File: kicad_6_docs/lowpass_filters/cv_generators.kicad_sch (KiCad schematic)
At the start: 28 parts, among them U6 TL072, U7 TL072

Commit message: Initial filter board layout
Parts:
- R1, R10: value 100k -> 330k
- R11, R2: value 330k -> 680k
- RV1, RV3, RV4: value 10k -> 100k
- RV2: value 10k_C.D. -> 100k_C.D.
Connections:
- net +5VA renamed +15V
- net -5VA renamed -15V
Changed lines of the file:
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@@
       (effects (font (size 1.27 1.27)) (justify right))
     )
-    (property "Value" "10k" (id 1) (at 43.18 123.1899 0)
+    (property "Value" "100k" (id 1) (at 43.18 123.1899 0)
       (effects (font (size 1.27 1.27)) (justify right))
     )
@@
       (effects (font (size 1.27 1.27)) (justify right))
     )
-    (property "Value" "10k" (id 1) (at 43.18 162.5599 0)
+    (property "Value" "100k" (id 1) (at 43.18 162.5599 0)
       (effects (font (size 1.27 1.27)) (justify right))
     )
@@
     (pin "3")
   )
+  (symbol (lib_id "power:-15V") (at 45.72 87.63 180) (unit 1)
+    (in_bom yes) (on_board yes) (fields_autoplaced)
+    (property "Reference" "#PWR?" (id 0) (at 45.72 90.17 0)
+      (effects (font (size 1.27 1.27)) hide)
+    )
+    (property "Value" "-15V" (id 1) (at 45.72 92.71 0))
+    (property "Footprint" "" (id 2) (at 45.72 87.63 0)
+      (effects (font (size 1.27 1.27)) hide)
+    )
+    (property "Datasheet" "" (id 3) (at 45.72 87.63 0)
+      (effects (font (size 1.27 1.27)) hide)
+    )
+    (pin "1")
+  )
   (symbol (lib_id "Device:R_Potentiometer") (at 45.72 81.28 0) (mirror x) (unit 1)
     (in_bom yes) (on_board yes) (fields_autoplaced)
@@
       (effects (font (size 1.27 1.27)) (justify right))
     )
-    (property "Value" "10k_C.D." (id 1) (at 43.18 82.5499 0)
+    (property "Value" "100k_C.D." (id 1) (at 43.18 82.5499 0)
       (effects (font (size 1.27 1.27)) (justify right))
     )
@@
     (pin "2")
   )
+  (symbol (lib_id "power:+15V") (at 45.72 106.68 0) (unit 1)
+    (in_bom yes) (on_board yes) (fields_autoplaced)
+    (property "Reference" "#PWR?" (id 0) (at 45.72 110.49 0)
+      (effects (font (size 1.27 1.27)) hide)
+    )
+    (property "Value" "+15V" (id 1) (at 45.72 101.6 0))
+    (property "Footprint" "" (id 2) (at 45.72 106.68 0)
+      (effects (font (size 1.27 1.27)) hide)
+    )
+    (property "Datasheet" "" (id 3) (at 45.72 106.68 0)
+      (effects (font (size 1.27 1.27)) hide)
+    )
+    (pin "1")
+  )
   (symbol (lib_id "Device:R") (at 142.24 63.5 90) (unit 1)
     (in_bom yes) (on_board yes) (fields_autoplaced)
@@
     (pin "2")
   )
-  (symbol (lib_id "power:+5VA") (at 45.72 41.91 0) (unit 1)
-    (in_bom yes) (on_board yes) (fields_autoplaced)
-    (property "Reference" "#PWR03" (id 0) (at 45.72 45.72 0)
-      (effects (font (size 1.27 1.27)) hide)
-    )
-    (property "Value" "+5VA" (id 1) (at 45.72 36.83 0))
-    (property "Footprint" "" (id 2) (at 45.72 41.91 0)
-      (effects (font (size 1.27 1.27)) hide)
-    )
-    (property "Datasheet" "" (id 3) (at 45.72 41.91 0)
-      (effects (font (size 1.27 1.27)) hide)
-    )
-    (pin "1")
-  )
   (symbol (lib_id "Device:R") (at 121.92 74.93 90) (unit 1)
     (in_bom yes) (on_board yes) (fields_autoplaced)
@@
     (pin "2")
   )
-  (symbol (lib_id "power:+5VA") (at 45.72 106.68 0) (unit 1)
-    (in_bom yes) (on_board yes) (fields_autoplaced)
-    (property "Reference" "#PWR09" (id 0) (at 45.72 110.49 0)
-      (effects (font (size 1.27 1.27)) hide)
-    )
-    (property "Value" "+5VA" (id 1) (at 45.72 101.6 0))
-    (property "Footprint" "" (id 2) (at 45.72 106.68 0)
-      (effects (font (size 1.27 1.27)) hide)
-    )
-    (property "Datasheet" "" (id 3) (at 45.72 106.68 0)
-      (effects (font (size 1.27 1.27)) hide)
-    )
-    (pin "1")
-  )
-  (symbol (lib_id "power:-5VA") (at 45.72 54.61 180) (unit 1)
-    (in_bom yes) (on_board yes) (fields_autoplaced)
-    (property "Reference" "#PWR04" (id 0) (at 45.72 57.15 0)
-      (effects (font (size 1.27 1.27)) hide)
-    )
-    (property "Value" "-5VA" (id 1) (at 45.72 59.69 0))
-    (property "Footprint" "" (id 2) (at 45.72 54.61 0)
-      (effects (font (size 1.27 1.27)) hide)
-    )
-    (property "Datasheet" "" (id 3) (at 45.72 54.61 0)
-      (effects (font (size 1.27 1.27)) hide)
-    )
-    (pin "1")
-  )
   (symbol (lib_id "Device:R") (at 121.92 40.64 90) (unit 1)
     (in_bom yes) (on_board yes) (fields_autoplaced)
     (property "Reference" "R2" (id 0) (at 121.92 34.29 90))
-    (property "Value" "330k" (id 1) (at 121.92 36.83 90))
+    (property "Value" "680k" (id 1) (at 121.92 36.83 90))
     (property "Footprint" "Resistor_SMD:R_0805_2012Metric" (id 2) (at 121.92 42.418 90)
       (effects (font (size 1.27 1.27)) hide)
@@
     (pin "2")
   )
+  (symbol (lib_id "power:+15V") (at 45.72 41.91 0) (unit 1)
+    (in_bom yes) (on_board yes) (fields_autoplaced)
+    (property "Reference" "#PWR?" (id 0) (at 45.72 45.72 0)
+      (effects (font (size 1.27 1.27)) hide)
+    )
+    (property "Value" "+15V" (id 1) (at 45.72 36.83 0))
+    (property "Footprint" "" (id 2) (at 45.72 41.91 0)
+      (effects (font (size 1.27 1.27)) hide)
+    )
+    (property "Datasheet" "" (id 3) (at 45.72 41.91 0)
+      (effects (font (size 1.27 1.27)) hide)
+    )
+    (pin "1")
+  )
   (symbol (lib_id "power:GND") (at 45.72 128.27 0) (unit 1)
     (in_bom yes) (on_board yes) (fields_autoplaced)
@@
     (pin "2")
   )
-  (symbol (lib_id "power:+5VA") (at 45.72 146.05 0) (unit 1)
-    (in_bom yes) (on_board yes) (fields_autoplaced)
-    (property "Reference" "#PWR011" (id 0) (at 45.72 149.86 0)
-      (effects (font (size 1.27 1.27)) hide)
-    )
-    (property "Value" "+5VA" (id 1) (at 45.72 140.97 0))
+  (symbol (lib_id "power:+15V") (at 45.72 146.05 0) (unit 1)
+    (in_bom yes) (on_board yes) (fields_autoplaced)
+    (property "Reference" "#PWR?" (id 0) (at 45.72 149.86 0)
+      (effects (font (size 1.27 1.27)) hide)
+    )
+    (property "Value" "+15V" (id 1) (at 45.72 140.97 0))
     (property "Footprint" "" (id 2) (at 45.72 146.05 0)
       (effects (font (size 1.27 1.27)) hide)
@@
     (pin "8")
   )
-  (symbol (lib_id "power:-5VA") (at 45.72 87.63 180) (unit 1)
-    (in_bom yes) (on_board yes) (fields_autoplaced)
-    (property "Reference" "#PWR08" (id 0) (at 45.72 90.17 0)
-      (effects (font (size 1.27 1.27)) hide)
-    )
-    (property "Value" "-5VA" (id 1) (at 45.72 92.71 0))
-    (property "Footprint" "" (id 2) (at 45.72 87.63 0)
-      (effects (font (size 1.27 1.27)) hide)
-    )
-    (property "Datasheet" "" (id 3) (at 45.72 87.63 0)
-      (effects (font (size 1.27 1.27)) hide)
-    )
-    (pin "1")
-  )
   (symbol (lib_id "Device:R") (at 142.24 137.16 90) (unit 1)
     (in_bom yes) (on_board yes) (fields_autoplaced)
@@
     (in_bom yes) (on_board yes) (fields_autoplaced)
     (property "Reference" "R11" (id 0) (at 162.56 107.95 90))
-    (property "Value" "330k" (id 1) (at 162.56 110.49 90))
+    (property "Value" "680k" (id 1) (at 162.56 110.49 90))
     (property "Footprint" "Resistor_SMD:R_0805_2012Metric" (id 2) (at 162.56 116.078 90)
       (effects (font (size 1.27 1.27)) hide)
@@
     (in_bom yes) (on_board yes) (fields_autoplaced)
     (property "Reference" "R10" (id 0) (at 121.92 107.95 90))
-    (property "Value" "100k" (id 1) (at 121.92 110.49 90))
+    (property "Value" "330k" (id 1) (at 121.92 110.49 90))
     (property "Footprint" "Resistor_SMD:R_0805_2012Metric" (id 2) (at 121.92 116.078 90)
       (effects (font (size 1.27 1.27)) hide)
@@
       (effects (font (size 1.27 1.27)) (justify right))
     )
-    (property "Value" "10k" (id 1) (at 43.18 49.5299 0)
+    (property "Value" "100k" (id 1) (at 43.18 49.5299 0)
       (effects (font (size 1.27 1.27)) (justify right))
     )
@@
     (pin "2")
   )
-  (symbol (lib_id "power:+5VA") (at 45.72 74.93 0) (unit 1)
-    (in_bom yes) (on_board yes) (fields_autoplaced)
-    (property "Reference" "#PWR05" (id 0) (at 45.72 78.74 0)
-      (effects (font (size 1.27 1.27)) hide)
-    )
-    (property "Value" "+5VA" (id 1) (at 45.72 69.85 0))
-    (property "Footprint" "" (id 2) (at 45.72 74.93 0)
-      (effects (font (size 1.27 1.27)) hide)
-    )
-    (property "Datasheet" "" (id 3) (at 45.72 74.93 0)
+  (symbol (lib_id "power:-15V") (at 45.72 54.61 180) (unit 1)
+    (in_bom yes) (on_board yes) (fields_autoplaced)
+    (property "Reference" "#PWR?" (id 0) (at 45.72 57.15 0)
+      (effects (font (size 1.27 1.27)) hide)
+    )
+    (property "Value" "-15V" (id 1) (at 45.72 59.69 0))
+    (property "Footprint" "" (id 2) (at 45.72 54.61 0)
+      (effects (font (size 1.27 1.27)) hide)
+    )
+    (property "Datasheet" "" (id 3) (at 45.72 54.61 0)
       (effects (font (size 1.27 1.27)) hide)
     )
@@
     (in_bom yes) (on_board yes) (fields_autoplaced)
     (property "Reference" "R1" (id 0) (at 121.92 22.86 90))
-    (property "Value" "100k" (id 1) (at 121.92 25.4 90))
+    (property "Value" "330k" (id 1) (at 121.92 25.4 90))
     (property "Footprint" "Resistor_SMD:R_0805_2012Metric" (id 2) (at 121.92 30.988 90)
       (effects (font (size 1.27 1.27)) hide)
@@
     (pin "2")
   )
+  (symbol (lib_id "power:+15V") (at 45.72 74.93 0) (unit 1)
+    (in_bom yes) (on_board yes) (fields_autoplaced)
+    (property "Reference" "#PWR?" (id 0) (at 45.72 78.74 0)
+      (effects (font (size 1.27 1.27)) hide)
+    )
+    (property "Value" "+15V" (id 1) (at 45.72 69.85 0))
+    (property "Footprint" "" (id 2) (at 45.72 74.93 0)
+      (effects (font (size 1.27 1.27)) hide)
+    )
+    (property "Datasheet" "" (id 3) (at 45.72 74.93 0)
+      (effects (font (size 1.27 1.27)) hide)
+    )
+    (pin "1")
+  )
 )

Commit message: Filter board rev 0 and outputs
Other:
- title: (none) -> M.S.M. Stereo Lowpass Filter Pedal
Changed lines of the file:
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@@
 (kicad_sch (version 20211123) (generator eeschema)
   (paper "A4")
+  (title_block
+    (title "M.S.M. Stereo Lowpass Filter Pedal")
+    (date "2022-05-24")
+    (rev "0")
+    (comment 2 "creativecommons.org/licenses/by/4.0")
+    (comment 3 "License: CC by 4.0")
+    (comment 4 "Author: Jordan Aceto")
+  )
   (junction (at 132.08 137.16) (diameter 0) (color 0 0 0 0)
   )
@@
   (symbol (lib_id "power:-15V") (at 45.72 87.63 180) (unit 1)
     (in_bom yes) (on_board yes) (fields_autoplaced)
-    (property "Reference" "#PWR?" (id 0) (at 45.72 90.17 0)
+    (property "Reference" "#PWR05" (id 0) (at 45.72 90.17 0)
       (effects (font (size 1.27 1.27)) hide)
     )
@@
   (symbol (lib_id "power:+15V") (at 45.72 106.68 0) (unit 1)
     (in_bom yes) (on_board yes) (fields_autoplaced)
-    (property "Reference" "#PWR?" (id 0) (at 45.72 110.49 0)
+    (property "Reference" "#PWR08" (id 0) (at 45.72 110.49 0)
       (effects (font (size 1.27 1.27)) hide)
     )
@@
   (symbol (lib_id "power:+15V") (at 45.72 41.91 0) (unit 1)
     (in_bom yes) (on_board yes) (fields_autoplaced)
-    (property "Reference" "#PWR?" (id 0) (at 45.72 45.72 0)
+    (property "Reference" "#PWR02" (id 0) (at 45.72 45.72 0)
       (effects (font (size 1.27 1.27)) hide)
     )
@@
   (symbol (lib_id "power:+15V") (at 45.72 146.05 0) (unit 1)
     (in_bom yes) (on_board yes) (fields_autoplaced)
-    (property "Reference" "#PWR?" (id 0) (at 45.72 149.86 0)
+    (property "Reference" "#PWR09" (id 0) (at 45.72 149.86 0)
       (effects (font (size 1.27 1.27)) hide)
     )
@@
   (symbol (lib_id "power:-15V") (at 45.72 54.61 180) (unit 1)
     (in_bom yes) (on_board yes) (fields_autoplaced)
-    (property "Reference" "#PWR?" (id 0) (at 45.72 57.15 0)
+    (property "Reference" "#PWR03" (id 0) (at 45.72 57.15 0)
       (effects (font (size 1.27 1.27)) hide)
     )
@@
   (symbol (lib_id "power:+15V") (at 45.72 74.93 0) (unit 1)
     (in_bom yes) (on_board yes) (fields_autoplaced)
-    (property "Reference" "#PWR?" (id 0) (at 45.72 78.74 0)
-      (effects (font (size 1.27 1.27)) hide)
-    )
+    (property "Reference" "#PWR04" (id 0) (at 45.72 78.74 0)
+      (effects (font (size 1.27 1.27)) hide)
+    )

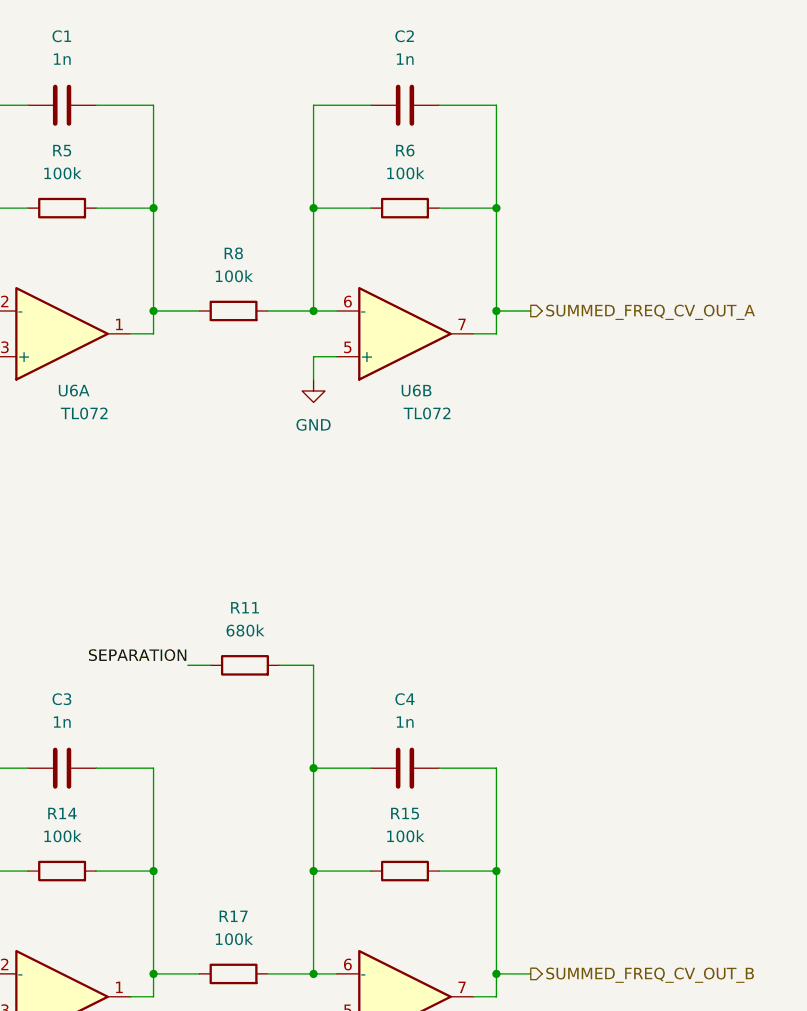
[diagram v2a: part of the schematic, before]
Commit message: Tweak some filter board values
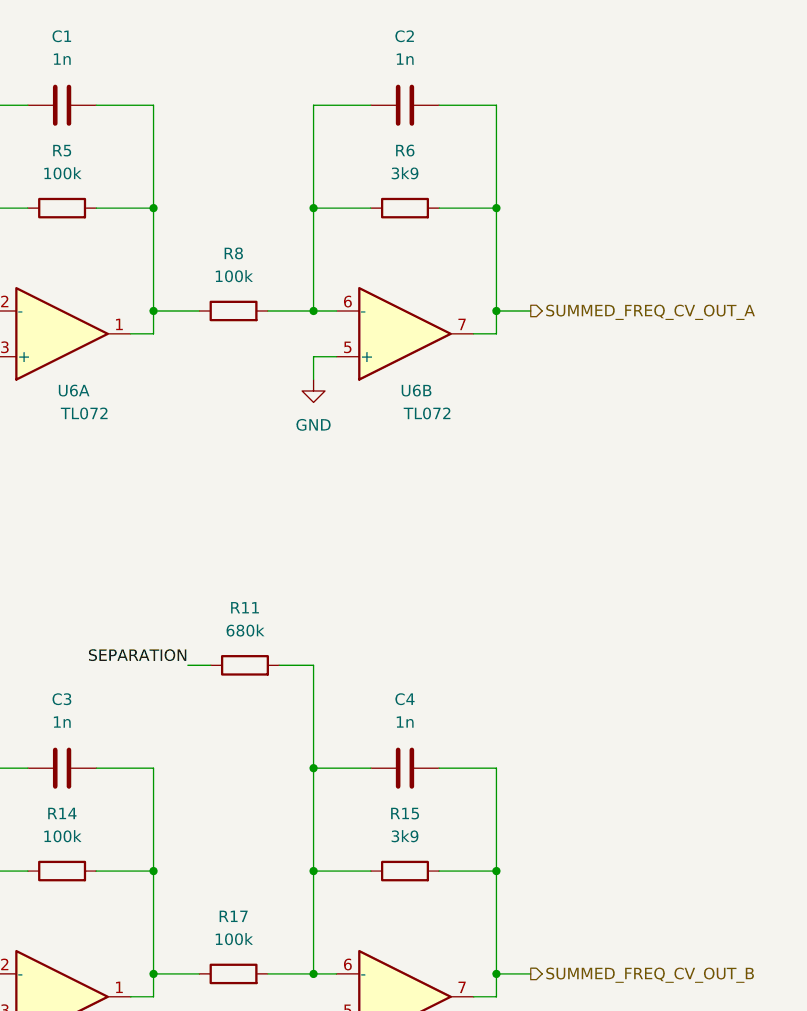
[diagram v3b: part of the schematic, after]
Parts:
- R15, R6: value 100k -> 3k9
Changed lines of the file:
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@@
   (title_block
     (title "M.S.M. Stereo Lowpass Filter Pedal")
-    (date "2022-05-24")
+    (date "2022-06-16")
     (rev "0")
     (comment 2 "creativecommons.org/licenses/by/4.0")
@@
     (in_bom yes) (on_board yes) (fields_autoplaced)
     (property "Reference" "R6" (id 0) (at 180.34 57.15 90))
-    (property "Value" "100k" (id 1) (at 180.34 59.69 90))
+    (property "Value" "3k9" (id 1) (at 180.34 59.69 90))
     (property "Footprint" "Resistor_SMD:R_0805_2012Metric" (id 2) (at 180.34 65.278 90)
       (effects (font (size 1.27 1.27)) hide)
@@
     (in_bom yes) (on_board yes) (fields_autoplaced)
     (property "Reference" "R15" (id 0) (at 180.34 130.81 90))
-    (property "Value" "100k" (id 1) (at 180.34 133.35 90))
+    (property "Value" "3k9" (id 1) (at 180.34 133.35 90))
     (property "Footprint" "Resistor_SMD:R_0805_2012Metric" (id 2) (at 180.34 138.938 90)
       (effects (font (size 1.27 1.27)) hide)
